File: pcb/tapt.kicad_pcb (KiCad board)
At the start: 4 copper layers, 28.3 x 28.3 mm, 37 parts, among them J1 Conn_01x05_Pin, J2 Conn_01x04_MountingPin, SW1 SW_SPDT_LIMIT, SW2 SW_SPST, U1 nRF52810-QCxx, Y1 32MHz, Y2 32.768kHz

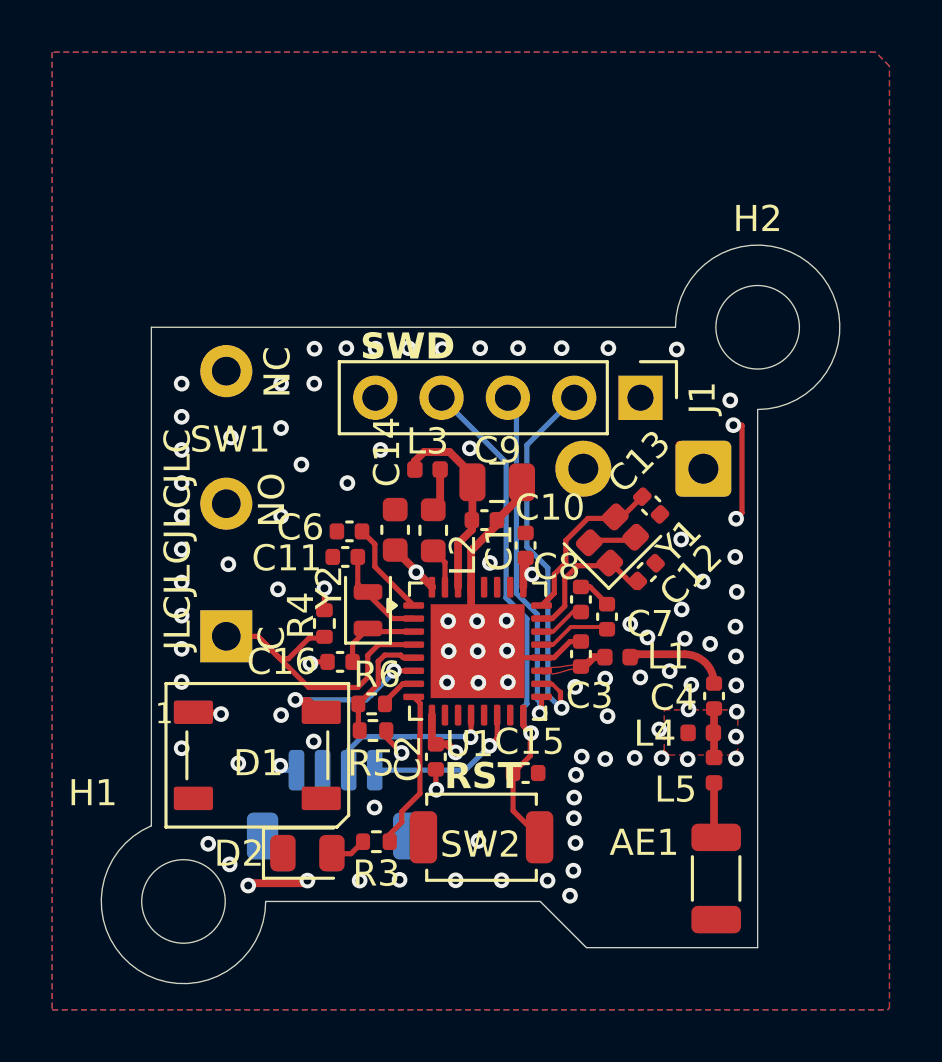
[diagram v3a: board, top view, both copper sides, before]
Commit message: pcb: impedance matching fixes
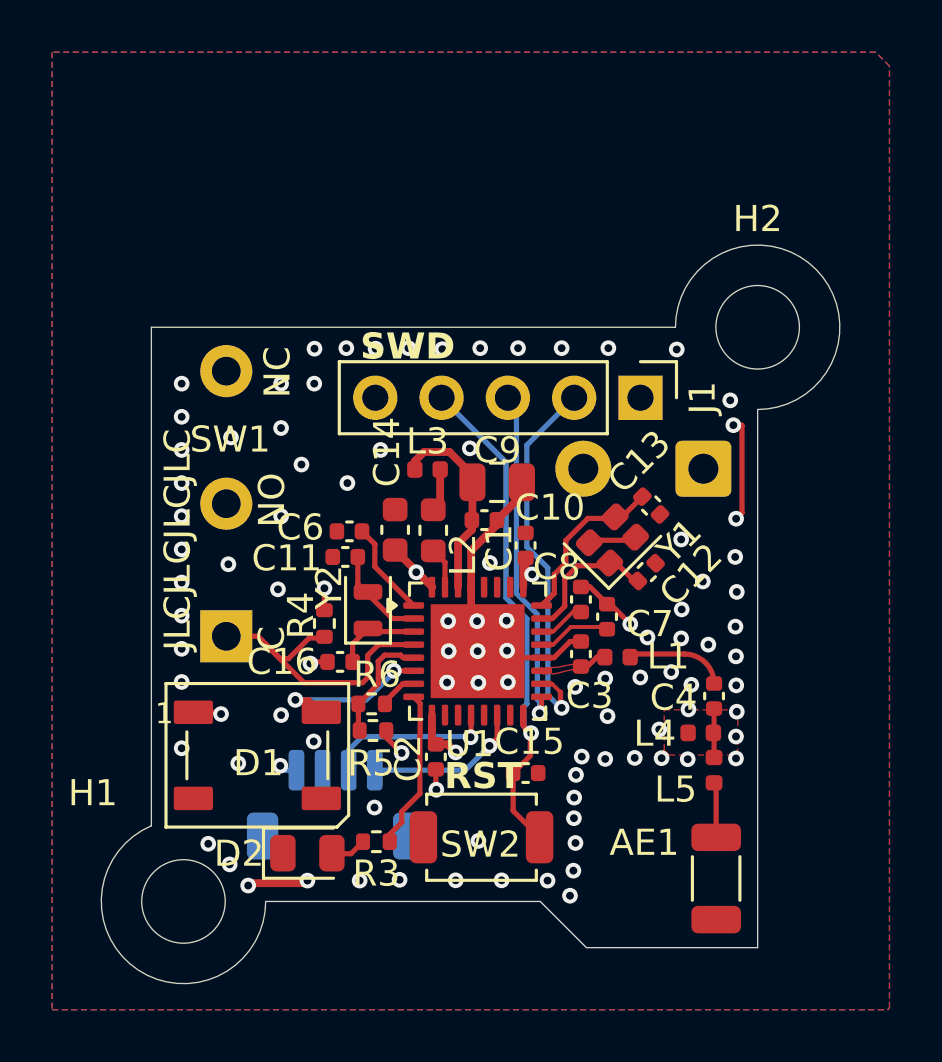
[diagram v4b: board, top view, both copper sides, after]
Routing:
- net VDD: track 10.9 -> 9.64 mm
- net SWDCLK: track 13.3 -> 12.4 mm
- net GND: track 21.8 -> 22.5 mm
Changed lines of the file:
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@@
 	)
 	(segment
-		(start 107.16 77.915)
-		(end 107.16 79.925)
-		(width 0.2939)
-		(layer "F.Cu")
-		(net 1)
-	)
-	(segment
-		(start 107.16 79.925)
-		(end 107.24 80.005)
-		(width 0.2939)
+		(start 107.24 80.005)
+		(end 107.24 77.995)
+		(width 0.1994)
 		(layer "F.Cu")
 		(net 1)
@@
 	)
 	(segment
-		(start 103.06 71.06)
-		(end 103.06 71.17)
-		(width 0.2)
-		(layer "F.Cu")
-		(net 3)
-	)
-	(segment
 		(start 100.55 73.12)
 		(end 98.35 73.12)
@@
 	)
 	(segment
-		(start 92.64 69.32)
-		(end 92.64 69.43)
-		(width 0.2)
-		(layer "F.Cu")
-		(net 3)
-	)
-	(segment
 		(start 92.35 73.28)
 		(end 91.75853 73.28)
@@
 	)
 	(segment
-		(start 104.09 68.62)
-		(end 104.149949 68.560051)
+		(start 103.19 71.07)
+		(end 103.95 71.83)
 		(width 0.2)
 		(layer "F.Cu")
@@
 	)
 	(segment
-		(start 102.382183 68.772183)
-		(end 102.534366 68.62)
-		(width 0.2)
-		(layer "F.Cu")
-		(net 3)
-	)
-	(segment
 		(start 89.4 81.76)
 		(end 89.31 81.85)
@@
 	)
 	(segment
+		(start 103.06 71.07)
+		(end 103.19 71.07)
+		(width 0.2)
+		(layer "F.Cu")
+		(net 3)
+	)
+	(segment
 		(start 108.210936 64.210936)
 		(end 107.9 64.210936)
@@
 	)
 	(via
-		(at 107.01 72.59)
-		(size 0.6)
-		(drill 0.3)
-		(layers "F.Cu" "B.Cu")
-		(free yes)
-		(net 3)
-	)
-	(via
-		(at 106.04 72.39)
+		(at 106.94 72.62)
+		(size 0.6)
+		(drill 0.3)
+		(layers "F.Cu" "B.Cu")
+		(free yes)
+		(net 3)
+	)
+	(via
+		(at 105.9 72.3803)
 		(size 0.6)
 		(drill 0.3)
@@
 	)
 	(via
-		(at 105.46 73.63695)
+		(at 105.52 73.67)
 		(size 0.6)
 		(drill 0.3)
@@
 	)
 	(segment
-		(start 105.83 64.96)
-		(end 106.75 65.88)
-		(width 0.3)
-		(layer "F.Cu")
-		(net 4)
-	)
-	(segment
 		(start 100.19 69.93)
 		(end 100.104017 69.844017)
@@
 	)
 	(segment
-		(start 102.19 73.46)
-		(end 102.55 73.1)
-		(width 0.2939)
+		(start 102.06 73.46)
+		(end 102.31 73.46)
+		(width 0.1994)
 		(layer "F.Cu")
 		(net 5)
 	)
 	(segment
-		(start 102.06 73.46)
-		(end 102.19 73.46)
-		(width 0.2939)
+		(start 102.67 73.1)
+		(end 102.975 73.1)
+		(width 0.1994)
 		(layer "F.Cu")
 		(net 5)
 	)
 	(segment
-		(start 102.55 73.1)
-		(end 102.975 73.1)
-		(width 0.2939)
+		(start 102.31 73.46)
+		(end 102.67 73.1)
+		(width 0.1994)
 		(layer "F.Cu")
 		(net 5)
 	)
 	(segment
-		(start 107.037106 73.987106)
+		(start 106.03 72.98)
+		(end 104.065 72.98)
+		(width 0.1994)
+		(layer "F.Cu")
+		(net 6)
+	)
+	(arc
+		(start 106.03 72.98)
+		(mid 106.82903 73.310969)
 		(end 107.16 74.11)
-		(width 0.1483)
-		(layer "F.Cu")
-		(net 6)
-	)
-	(segment
-		(start 107.16 74.11)
-		(end 107.16 74.11)
-		(width 0.1483)
-		(layer "F.Cu")
-		(net 6)
-	)
-	(segment
-		(start 107.16 74.11)
-		(end 107.16 74.11)
-		(width 0.2939)
-		(layer "F.Cu")
-		(net 6)
-	)
-	(segment
-		(start 104.045 73.18)
-		(end 104.235 72.99)
-		(width 0.2939)
-		(layer "F.Cu")
-		(net 6)
-	)
-	(segment
-		(start 106.04 72.99)
-		(end 104.235 72.99)
-		(width 0.2939)
-		(layer "F.Cu")
-		(net 6)
-	)
-	(arc
-		(start 106.04 72.99)
-		(mid 106.831959 73.31804)
-		(end 107.16 74.11)
-		(width 0.2939)
+		(width 0.1994)
 		(layer "F.Cu")
 		(net 6)
@@
 	)
 	(segment
-		(start 103.114701 69.595299)
-		(end 103.16 69.55)
+		(start 103.271178 69.55)
+		(end 103.47 69.55)
 		(width 0.2)
 		(layer "F.Cu")
@@
 	)
 	(segment
+		(start 103.47 69.55)
+		(end 104.150589 70.230589)
+		(width 0.2)
+		(layer "F.Cu")
+		(net 12)
+	)
+	(segment
 		(start 101.44 70.09245)
 		(end 101.937151 69.595299)
@@
 	)
 	(segment
-		(start 103.271178 69.55)
-		(end 104.150589 70.429411)
-		(width 0.2)
-		(layer "F.Cu")
-		(net 12)
-	)
-	(segment
 		(start 101.44 71.145798)
 		(end 101.44 70.09245)
@@
 	)
 	(segment
-		(start 103.16 69.55)
-		(end 103.271178 69.55)
-		(width 0.2)
-		(layer "F.Cu")
-		(net 12)
-	)
-	(segment
 		(start 101.937151 69.595299)
 		(end 103.114701 69.595299)
@@
 	)
 	(segment
+		(start 91.45 74.08)
+		(end 89.69 72.32)
+		(width 0.2)
+		(layer "F.Cu")
+		(net 18)
+	)
+	(segment
+		(start 90.85 73.16)
+		(end 90.53 73.16)
+		(width 0.2)
+		(layer "F.Cu")
+		(net 18)
+	)
+	(segment
+		(start 89.69 72.32)
+		(end 89.67 72.3)
+		(width 0.2)
+		(layer "F.Cu")
+		(net 18)
+	)
+	(segment
+		(start 91.641 72.369)
+		(end 90.85 73.16)
+		(width 0.2)
+		(layer "F.Cu")
+		(net 18)
+	)
+	(segment
+		(start 92.181 72.369)
+		(end 91.641 72.369)
+		(width 0.2)
+		(layer "F.Cu")
+		(net 18)
+	)
+	(segment
+		(start 95.65 72.62)
+		(end 94.3 72.62)
+		(width 0.2)
+		(layer "F.Cu")
+		(net 18)
+	)
+	(segment
+		(start 90.53 73.16)
+		(end 89.69 72.32)
+		(width 0.2)
+		(layer "F.Cu")
+		(net 18)
+	)
+	(segment
 		(start 94.3 72.62)
 		(end 93.891 73.029)
@@
 	)
 	(segment
-		(start 90.85 73.16)
-		(end 90.53 73.16)
-		(width 0.2)
-		(layer "F.Cu")
-		(net 18)
-	)
-	(segment
-		(start 89.69 72.32)
-		(end 89.67 72.3)
-		(width 0.2)
-		(layer "F.Cu")
-		(net 18)
-	)
-	(segment
-		(start 91.641 72.369)
-		(end 90.85 73.16)
-		(width 0.2)
-		(layer "F.Cu")
-		(net 18)
-	)
-	(segment
 		(start 93.891 73.029)
 		(end 93.891 73.879)
@@
 	)
 	(segment
+		(start 93.69 74.08)
+		(end 91.45 74.08)
+		(width 0.2)
+		(layer "F.Cu")
+		(net 18)
+	)
+	(segment
 		(start 93.891 73.879)
-		(end 93.51 74.26)
-		(width 0.2)
-		(layer "F.Cu")
-		(net 18)
-	)
-	(segment
-		(start 92.181 72.369)
-		(end 91.641 72.369)
-		(width 0.2)
-		(layer "F.Cu")
-		(net 18)
-	)
-	(segment
-		(start 90.53 73.16)
-		(end 89.69 72.32)
-		(width 0.2)
-		(layer "F.Cu")
-		(net 18)
-	)
-	(segment
-		(start 91.63 74.26)
-		(end 89.69 72.32)
-		(width 0.2)
-		(layer "F.Cu")
-		(net 18)
-	)
-	(segment
-		(start 92.23 72.32)
-		(end 92.181 72.369)
-		(width 0.2)
-		(layer "F.Cu")
-		(net 18)
-	)
-	(segment
-		(start 95.65 72.62)
-		(end 94.3 72.62)
+		(end 93.69 74.08)
 		(width 0.2)
 		(layer "F.Cu")
@@
 		(start 89.67 72.3)
 		(end 88.47 72.3)
-		(width 0.2)
-		(layer "F.Cu")
-		(net 18)
-	)
-	(segment
-		(start 93.51 74.26)
-		(end 91.63 74.26)
 		(width 0.2)
 		(layer "F.Cu")
@@
 	)
 	(segment
-		(start 99.26 63.501)
-		(end 99.589 63.83)
-		(width 0.2)
-		(layer "B.Cu")
-		(net 24)
-	)
-	(segment
 		(start 99.589 63.83)
 		(end 99.589 70.661957)
@@
 	)
 	(segment
-		(start 99.26 63.16)
-		(end 99.26 63.501)
-		(width 0.2)
-		(layer "B.Cu")
-		(net 24)
-	)
-	(segment
 		(start 100.389 71.461957)
 		(end 100.389 74.721957)
@@
 	)
 	(segment
-		(start 94.02 72.12)
-		(end 93.9 72)
-		(width 0.2)
-		(layer "F.Cu")
-		(net 28)
-	)
-	(segment
 		(start 95.65 72.12)
 		(end 94.02 72.12)
@@
 	)
 	(segment
-		(start 93.53 75.86)
-		(end 93.58 75.91)
-		(width 0.2)
-		(layer "F.Cu")
-		(net 34)
-	)
-	(segment
 		(start 95.250001 73.12)
 		(end 95.65 73.12)
@@
 	)
 	(segment
-		(start 94.55 74.804202)
-		(end 94.55 74.89)
-		(width 0.2)
-		(layer "F.Cu")
-		(net 36)
-	)
-	(segment
 		(start 95.234202 74.12)
 		(end 94.55 74.804202)
@@
 		(start 107.16 76.945)
 		(end 107.16 75.07)
-		(width 0.2939)
+		(width 0.1994)
 		(layer "F.Cu")
 		(net 37)
@@
 		(layer "F.Cu")
 		(hatch edge 0.5)
+		(priority 17540)
 		(connect_pads yes
 			(clearance 0)
@@
 		(polygon
 			(pts
-				(xy 102.071122 73.46) (xy 102.068 73.38585) (xy 101.911586 73.388906) (xy 101.77649 73.397201) (xy 101.658435 73.409426)
-				(xy 101.553145 73.42427) (xy 101.456344 73.440425) (xy 101.363755 73.456579) (xy 101.271102 73.471423)
-				(xy 101.17411 73.483648) (xy 101.068501 73.491943) (xy 100.95 73.495) (xy 100.55 73.495) (xy 100.535084 73.62158)
-				(xy 100.563171 73.744304) (xy 100.963171 73.744304) (xy 101.080835 73.727621) (xy 101.185136 73.705383)
-				(xy 101.280487 73.679313) (xy 101.371299 73.651132) (xy 101.461987 73.622562) (xy 101.556962 73.595326)
-				(xy 101.660639 73.571144) (xy 101.777428 73.551739) (xy 101.911744 73.538834) (xy 102.068 73.53415)
+				(xy 102.074955 73.46) (xy 102.068 73.3603) (xy 101.911278 73.364071) (xy 101.776058 73.374308) (xy 101.658021 73.389395)
+				(xy 101.552846 73.407714) (xy 101.456214 73.42765) (xy 101.363805 73.447585) (xy 101.271299 73.465904)
+				(xy 101.174376 73.480991) (xy 101.068716 73.491228) (xy 100.95 73.495) (xy 100.55 73.495) (xy 100.535084 73.62158)
+				(xy 100.563171 73.744304) (xy 100.963171 73.744304) (xy 101.080489 73.728379) (xy 101.184709 73.708109)
+				(xy 101.280172 73.68491) (xy 101.371223 73.660202) (xy 101.462201 73.635404) (xy 101.55745 73.611933)
+				(xy 101.661313 73.591209) (xy 101.77813 73.574649) (xy 101.912245 73.563673) (xy 102.068 73.5597)
 			)
 		)

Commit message: pcb: update production files
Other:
- board text added: "05150ff"
- board text removed: "0123abc"
